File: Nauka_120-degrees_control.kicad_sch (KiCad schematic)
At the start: 0 parts

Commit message: VER1.0: накидал схему управления затворами
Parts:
- added C1, C2: 20p, Capacitor_SMD:C_0805_2012Metric_Pad1.18x1.45mm_HandSolder, symbol Device:C_Small
- added C3, C4, C5, C6, C7: 100n, Capacitor_SMD:C_0805_2012Metric_Pad1.18x1.45mm_HandSolder, symbol Device:C_Small
- added D1, D2: ~, Package_SO:SOIC-14_3.9x8.7mm_P1.27mm, symbol Logic_my:74HC32
- added R1: 10M, Resistor_SMD:R_0805_2012Metric_Pad1.20x1.40mm_HandSolder, symbol Device:R_Small
- added R2: 100k, Resistor_SMD:R_0805_2012Metric_Pad1.20x1.40mm_HandSolder, symbol Device:R_Small
- added R3, R4, R5, R6, R7, R8, R9: 0, Resistor_SMD:R_0805_2012Metric_Pad1.20x1.40mm_HandSolder, symbol Device:R_Small
- added U1: 4040, Package_SO:SO-16_3.9x9.9mm_P1.27mm, symbol 4xxx:4040
- added U2: 4017, Package_SO:SO-16_3.9x9.9mm_P1.27mm, symbol 4xxx:4017
- added U4: 74LVC2G04, symbol 74xGxx:74LVC2G04
- added Y1: 4.9152M, Crystal:Crystal_SMD_HC49-SD_HandSoldering, symbol Device:Crystal
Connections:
- new net: C1.2, R1.1, U4.1, Y1.2
- new net: R1.2, R2.1, U4.3, U4.6
- new net: C2.2, R2.2, Y1.1
- new net: R6.1, U1.14 (Q9)
- new net: R5.2, R6.2, R7.2, R8.2, U2.14 (CLK)
- new net: D1.1 (1A), D2.5 (Q10), U2.3 (Q0)
- new net: D1.10 (Q10), D2.4 (Q11), U2.1 (Q5)
- new net: D1.2 (1B), D2.10 (Q10), U2.2 (Q1)
- new net: D1.4 (Q11), D2.9 (Q11), U2.4 (Q2)
- new net: D1.5 (Q10), D2.2 (1B), U2.7 (Q3)
- new net: D1.9 (Q11), D2.1 (1A), U2.10 (Q4)
- new net: R9.1, U2.13 (CKEN)
- new net: U2.15 (Reset), U2.5 (Q6)
- new net: R8.1, U1.1 (Q11)
- new net: U1.10 (CLK), U4.4
- new net: R3.1, R4.1, U1.11 (Reset)
- new net: R5.1, U1.12 (Q8)
- new net: R7.1, U1.15 (Q10)
- new net +5V: C3.2, C4.2, C5.2, C6.2, C7.2, D1.14 (VCC), D2.14 (VCC), U1.16 (VDD), U2.16 (VDD), U4.5 (VCC)
- new net G1H: D1.3 (1Y)
- new net G1L: D2.3 (1Y)
- new net G2H: D1.6
- new net G2L: D2.6
- new net G3H: D1.8
- new net G3L: D2.8
- new net GND: C1.1, C2.1, C3.1, C4.1, C5.1, C6.1, C7.1, D1.7 (GND), D2.7 (GND), R3.2, R9.2, U1.8 (VSS), U2.8 (VSS), U4.2 (GND)
- new net Reset_4040: R4.2
- no-connect marks 0 -> 18

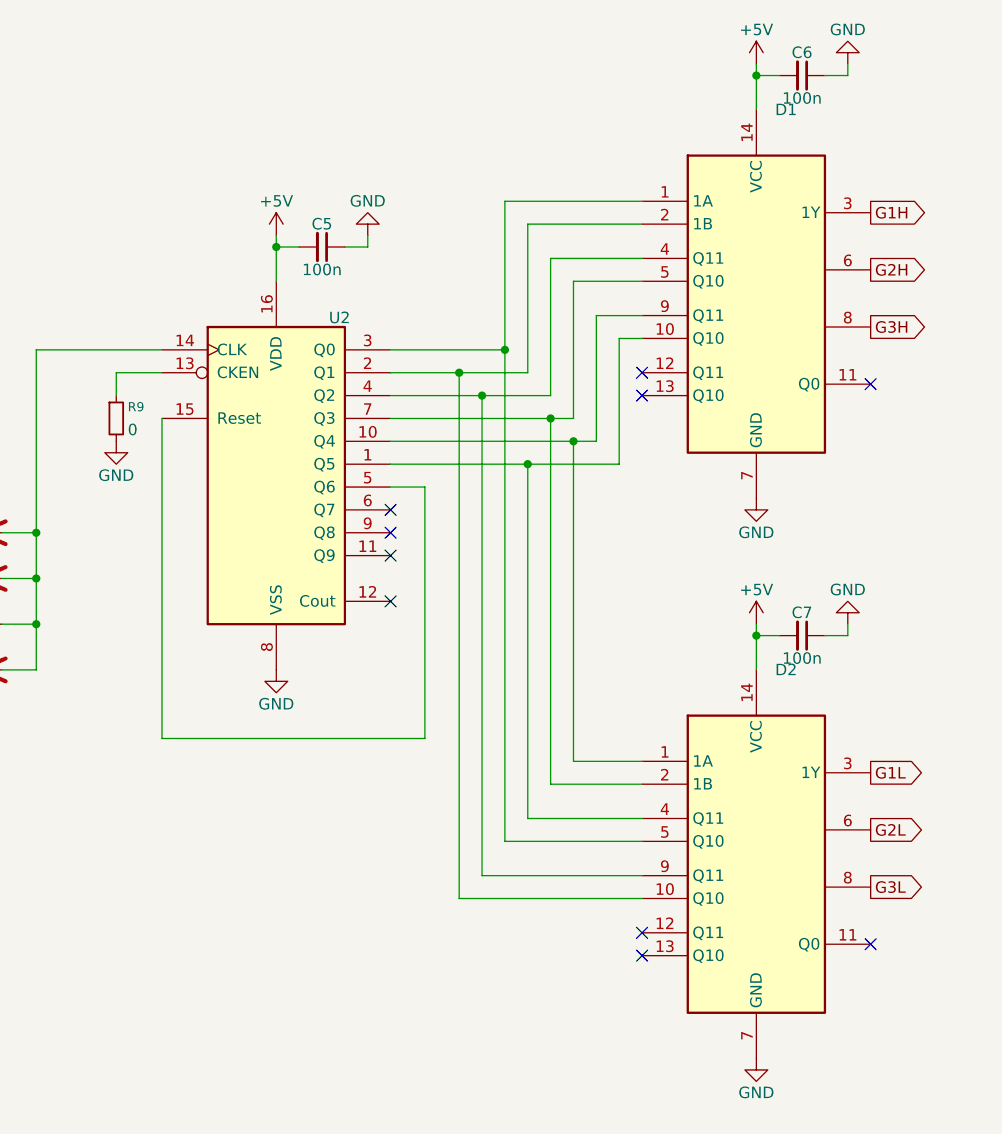
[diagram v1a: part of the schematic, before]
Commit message: VER1.0: изменил логические И на трехвходные И-НЕ
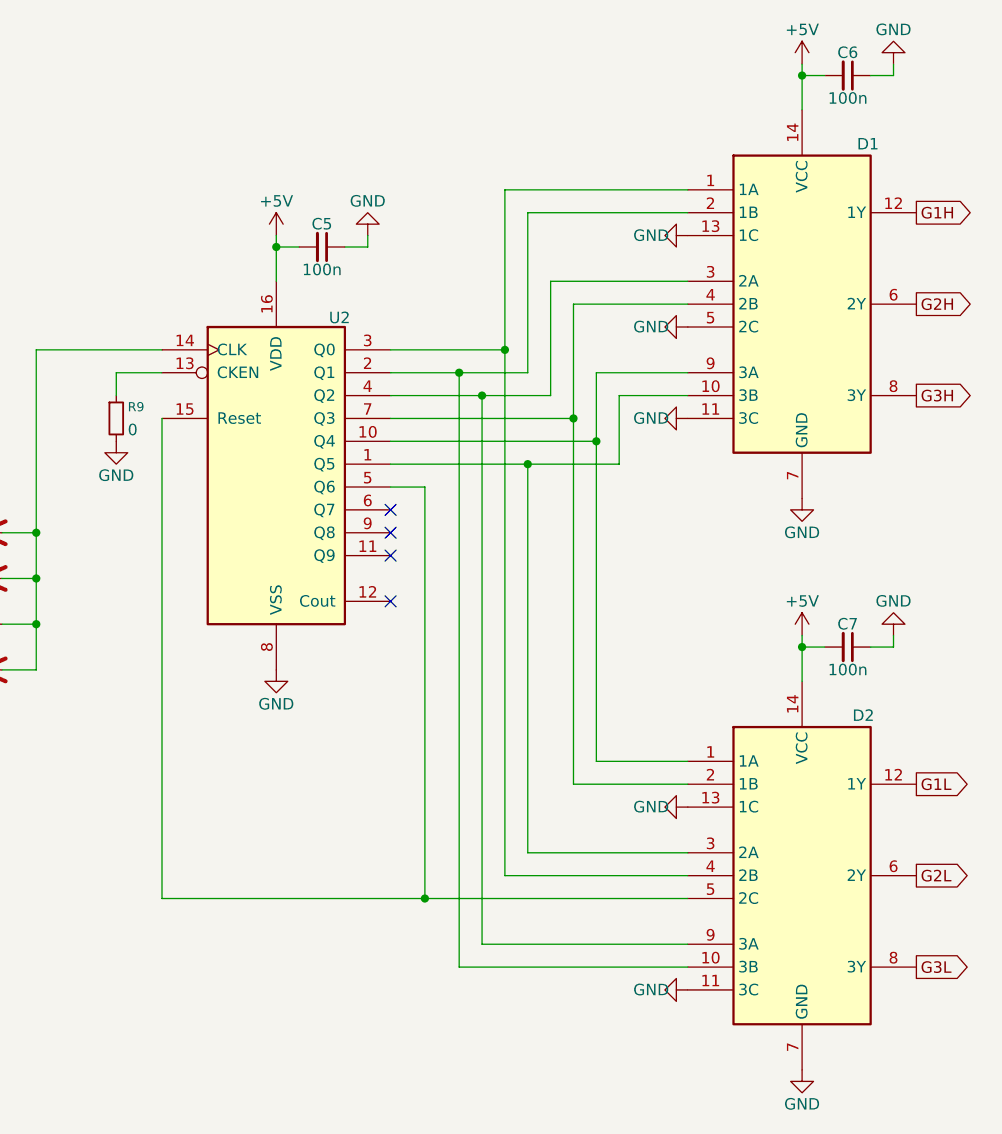
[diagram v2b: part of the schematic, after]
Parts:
- removed D1, D2: ~, Package_SO:SOIC-14_3.9x8.7mm_P1.27mm, symbol Logic_my:74HC32
- added D1, D2: ~, Package_SO:SOIC-14_3.9x8.7mm_P1.27mm, symbol Logic_my:74HC27D
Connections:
- net +5V: now also D1.14 (VCC), D2.14 (VCC)
- net G1H: now also D1.12 (1Y)
- net G1L: now also D2.12 (1Y)
- net G2H: now also D1.6 (2Y)
- net G2L: now also D2.6 (2Y)
- net G3H: now also D1.8 (3Y)
- net G3L: now also D2.8 (3Y)
- net GND: now also D1.11 (3C), D1.13 (1C), D1.5 (2C), D1.7 (GND), D2.11 (3C), D2.13 (1C), D2.7 (GND)
- net at U2.3 (Q0): now also D1.1 (1A), D2.4 (2B)
- net at U2.1 (Q5): now also D1.10 (3B), D2.3 (2A)
- net at U2.2 (Q1): now also D1.2 (1B), D2.10 (3B)
- net at U2.4 (Q2): now also D1.3 (2A), D2.9 (3A)
- net at U2.7 (Q3): now also D1.4 (2B), D2.2 (1B)
- net at U2.10 (Q4): now also D1.9 (3A), D2.1 (1A)
- net at U2.15 (Reset), U2.5 (Q6): now also D2.5 (2C)
- no-connect marks 18 -> 12
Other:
- moved on the sheet: C6, C7

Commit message: VER1.0: добавил драйвера
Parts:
- added C10, C11, C18, C19, C22, C23, C29, C30, C33, C34, C39, C40, C44, C45, C50, C51, C55, C56, C61, C62, C66, C67, C72, C73: 10u, Capacitor_SMD:C_1206_3216Metric_Pad1.33x1.80mm_HandSolder, symbol Device:C_Small
- added C13, C24, C35, C46, C57, C68: 2.2u, Capacitor_SMD:C_0805_2012Metric_Pad1.18x1.45mm_HandSolder, symbol Device:C_Small
- added C14, C25, C36, C47, C58, C69: 100p, Capacitor_SMD:C_0805_2012Metric_Pad1.18x1.45mm_HandSolder, symbol Device:C_Small
- added C15, C16, C20, C21, C42, C43, C53, C54, C6, C64, C65, C7: 4.7u, Capacitor_SMD:C_1206_3216Metric_Pad1.33x1.80mm_HandSolder, symbol Device:C_Small
- added C17, C26, C38, C48, C60, C70: 10n, Capacitor_SMD:C_0805_2012Metric_Pad1.18x1.45mm_HandSolder, symbol Device:C_Small
- added C27, C28, C31, C32, C37, C41, C49, C52, C59, C63, C71, C74: 56p, Capacitor_SMD:C_0805_2012Metric_Pad1.18x1.45mm_HandSolder, symbol Device:C_Small
- added C4: 100n, Capacitor_SMD:C_0805_2012Metric_Pad1.18x1.45mm_HandSolder, symbol Device:C_Small
- added D10, D12, D26, D33, D4, D40: NSI6651, Package_SO:SOIC-16W_7.5x10.3mm_P1.27mm, symbol Driver_My:NSI6651
- added D11, D2, D25, D32, D39, D9: ~, QAxCx, symbol Mornsun:QAxCx
- added D13, D14, D20, D21, D27, D28, D34, D35, D41, D42, D5, D6: D_Small, Diode_SMD:D_SMA_Handsoldering, symbol Device:D_Small
- added D15, D23, D30, D37, D44, D8: ~, Diode_SMD:D_SOD-123, symbol Device:D_Schottky_Small
- added D16, D17, D18, D19, D22, D24, D29, D31, D36, D38, D43, D45: ~, LED_SMD:LED_0805_2012Metric_Pad1.15x1.40mm_HandSolder, symbol Device:LED_Small
- added D3: ~, Package_SO:SO-14_3.9x8.65mm_P1.27mm, symbol Logic_my:74AHC14D
- added L1, L11, L3, L5, L7, L9: 12u, Inductor_SMD:L_1210_3225Metric_Pad1.42x2.65mm_HandSolder, symbol Device:L_Small
- added L10, L12, L2, L4, L6, L8: 47u, Inductor_SMD:L_1812_4532Metric_Pad1.30x3.40mm_HandSolder, symbol Device:L_Small
- added Q1, Q2, Q3, Q4, Q5, Q6: C2M0280120D, Package_TO_SOT_THT:TO-247-3_Horizontal_TabUp, symbol Transistor_FET:C2M0280120D
- added R10, R15, R20, R40, R50, R60: 510, Resistor_SMD:R_0805_2012Metric_Pad1.20x1.40mm_HandSolder, symbol Device:R_Small
- added R11, R16, R18, R21, R25, R27, R30, R33, R39, R41, R43, R49, R51, R53, R59, R61, R63, R69: 1k, Resistor_SMD:R_0805_2012Metric_Pad1.20x1.40mm_HandSolder, symbol Device:R_Small
- added R12, R17, R22, R42, R52, R62: Rdesat, Resistor_SMD:R_0805_2012Metric_Pad1.20x1.40mm_HandSolder, symbol Device:R_Small
- added R13, R14, R23, R24, R34, R35, R44, R45, R54, R55, R64, R65: 3, Resistor_SMD:R_0805_2012Metric_Pad1.20x1.40mm_HandSolder, symbol Device:R_Small
- added R19, R26, R29, R31, R36, R37, R46, R47, R56, R57, R66, R67: 10k, Resistor_SMD:R_0805_2012Metric_Pad1.20x1.40mm_HandSolder, symbol Device:R_Small
- added R28, R32, R38, R48, R58, R68: 560, Resistor_SMD:R_0805_2012Metric_Pad1.20x1.40mm_HandSolder, symbol Device:R_Small
- renumbered C6 to C1, C7 to C12, C4 to C2, C5 to C3, C3 to C5, C1 to C8, C2 to C9, D2 to D7, R9 to R3, R3 to R5, R5 to R6, R6 to R7, R7 to R8, R8 to R9, U4 to U1, U1 to U2, U2 to U3
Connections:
- net +5V: now also C13.2, C24.2, C35.2, C4.2, C46.2, C57.2, C68.2, D10.15 (Vcc1), D12.15 (Vcc1), D26.15 (Vcc1), D3.14 (VCC), D33.15 (Vcc1), D4.15 (Vcc1), D40.15 (Vcc1), R18.2, R25.2, R26.2, R27.2, R30.2, R31.2, R33.2, R36.2, R39.2, R43.2, R46.2, R49.2, R53.2, R56.2, R59.2, R63.2, R66.2, R69.2
- net G1H: now also D3.2 (1Y); no longer D1.12 (1Y)
- net G1L: now also D3.8 (4Y); no longer D7.12 (1Y)
- net G2H: now also D3.4 (2Y); no longer D1.6 (2Y)
- net G2L: now also D3.10 (5Y); no longer D7.6 (2Y)
- net G3H: now also D3.6 (3Y); no longer D1.8 (3Y)
- net G3L: now also D3.12 (6Y); no longer D7.8 (3Y)
- net GND: now also C13.1, C24.1, C27.2, C28.2, C31.2, C32.2, C35.1, C37.2, C4.1, C41.2, C46.1, C49.2, C52.2, C57.1, C59.2, C63.2, C68.1, C71.2, C74.2, D10.16 (TEST), D10.9 (GND1), D12.16 (TEST), D12.9 (GND1), D17.1 (K), D19.1 (K), D24.1 (K), D26.16 (TEST), D26.9 (GND1), D3.7 (GND), D31.1 (K), D33.16 (TEST), D33.9 (GND1), D38.1 (K), D4.16 (TEST), D4.9 (GND1), D40.16 (TEST), D40.9 (GND1), D45.1 (K)
- new net: D10.6 (OUTL), R35.1
- new net: D43.2 (A), R63.1
- new net: C37.1, D10.13 (~{FLT}), D22.1 (K), R36.1
- new net: D22.2 (A), R18.1
- new net: D36.2 (A), R53.1
- new net: D26.4 (OUTH), R44.1
- new net: C54.1, L10.1, L9.2
- new net: D32.1 (Vin), L10.2
- new net: C69.2, D40.2 (DESAT), D44.1 (K), R61.1
- new net: D5.1 (K), D6.2 (A)
- new net: D5.2 (A), R12.1
- new net: D17.2 (A), R28.1
- new net: C27.1, D12.12 (RDY), R25.1, R28.2
- new net: C21.1, L3.2, L4.1
- new net: D11.1 (Vin), L4.2
- new net: C36.2, D10.2 (DESAT), D23.1 (K), R16.1
- new net: D40.6 (OUTL), R65.1
- new net: C31.1, D18.1 (K), D4.13 (~{FLT}), R31.1
- new net: C52.1, D26.12 (RDY), R48.2, R49.1
- new net: C49.1, D26.13 (~{FLT}), D29.1 (K), R46.1
- new net: C47.2, D26.2 (DESAT), D30.1 (K), R41.1
- new net: D26.6 (OUTL), R45.1
- new net: D27.1 (K), D28.2 (A)
- new net: D27.2 (A), R42.1
- new net: R10.1, R11.2, R12.2
- new net: C7.1, L1.2, L2.1
- new net: D34.2 (A), R52.1
- new net: R50.1, R51.2, R52.2
- new net: C25.2, D12.2 (DESAT), D15.1 (K), R21.1
- new net: R60.1, R61.2, R62.2
- new net: C63.1, D33.12 (RDY), R58.2, R59.1
- new net: C16.1, L5.2, L6.1
- new net: D9.1 (Vin), L6.2
- new net: C65.1, L11.2, L12.1
- new net: D39.1 (Vin), L12.2
- new net: C41.1, D10.12 (RDY), R38.2, R39.1
- new net: D45.2 (A), R68.1
- new net: C43.1, L7.2, L8.1
- new net: C74.1, D40.12 (RDY), R68.2, R69.1
- new net: C71.1, D40.13 (~{FLT}), D43.1 (K), R66.1
- new net: D40.4 (OUTH), R64.1
- new net: D2.1 (Vin), L2.2
- new net: D41.2 (A), R62.1
- new net: D13.1 (K), D14.2 (A)
- new net: C14.2, D4.2 (DESAT), D8.1 (K), R11.1
- new net: C28.1, D12.13 (~{FLT}), D16.1 (K), R26.1
- new net: D12.4 (OUTH), R23.1
- new net: D12.6 (OUTL), R24.1
- new net: D18.2 (A), R30.1
- new net: C59.1, D33.13 (~{FLT}), D36.1 (K), R56.1
- new net: D19.2 (A), R32.1
- new net: C32.1, D4.12 (RDY), R32.2, R33.1
- new net: D16.2 (A), R27.1
- new net: D3.9 (4A), D7.12 (1Y)
- new net: D3.11 (5A), D7.6 (2Y)
- new net: D3.13 (6A), D7.8 (3Y)
- new net: R15.1, R16.2, R17.2
- new net: D31.2 (A), R48.1
- new net: D13.2 (A), R22.1
- new net: R40.1, R41.2, R42.2
- new net: R20.1, R21.2, R22.2
- new net: D24.2 (A), R38.1
- new net: D25.1 (Vin), L8.2
- new net: D1.12 (1Y), D3.1 (1A)
- new net: D1.6 (2Y), D3.3 (2A)
- new net: D1.8 (3Y), D3.5 (3A)
- new net: D20.2 (A), R17.1
- new net: C58.2, D33.2 (DESAT), D37.1 (K), R51.1
- new net: D41.1 (K), D42.2 (A)
- new net: D38.2 (A), R58.1
- new net: D4.4 (OUTH), R13.1
- new net: D4.6 (OUTL), R14.1
- new net: D33.4 (OUTH), R54.1
- new net: D29.2 (A), R43.1
- new net: D10.4 (OUTH), R34.1
- new net: D34.1 (K), D35.2 (A)
- new net: D20.1 (K), D21.2 (A)
- new net: D33.6 (OUTL), R55.1
- new net +15V: C15.1, C20.1, C42.1, C53.1, C6.1, C64.1, L1.1, L11.1, L3.1, L5.1, L7.1, L9.1
- new net +15VL: C22.2, C23.2, C44.2, C45.2, C66.2, C67.2, D11.7 (+Vo), D12.5 (Vcc2), D25.7 (+Vo), D26.5 (Vcc2), D39.7 (+Vo), D40.5 (Vcc2), R20.2, R40.2, R60.2
- new net +15V_H1: C10.2, C11.2, C33.2, C34.2, C55.2, C56.2, D10.5 (Vcc2), D2.7 (+Vo), D32.7 (+Vo), D33.5 (Vcc2), D4.5 (Vcc2), D9.7 (+Vo), R10.2, R15.2, R50.2
- new net -15VL: C29.1, C30.1, C50.1, C51.1, C72.1, C73.1, D11.5 (-Vo), D12.1 (Vee2), D12.8 (Vee2), D25.5 (-Vo), D26.1 (Vee2), D26.8 (Vee2), D39.5 (-Vo), D40.1 (Vee2), D40.8 (Vee2)
- new net -4V_H1: C18.1, C19.1, C39.1, C40.1, C61.1, C62.1, D10.1 (Vee2), D10.8 (Vee2), D2.5 (-Vo), D32.5 (-Vo), D33.1 (Vee2), D33.8 (Vee2), D4.1 (Vee2), D4.8 (Vee2), D9.5 (-Vo)
- new net GND1: C15.2, C16.2, C20.2, C21.2, C42.2, C43.2, C53.2, C54.2, C6.2, C64.2, C65.2, C7.2, D11.2 (GND), D2.2 (GND), D25.2 (GND), D32.2 (GND), D39.2 (GND), D9.2 (GND)
- new net GNDPWR: C22.1, C23.1, C25.1, C26.2, C29.2, C30.2, C44.1, C45.1, C47.1, C48.2, C50.2, C51.2, C66.1, C67.1, C69.1, C70.2, C72.2, C73.2, D11.6 (0V), D12.3 (GND2), D15.2 (A), D25.6 (0V), D26.3 (GND2), D30.2 (A), D39.6 (0V), D40.3 (GND2), D44.2 (A), Q2.3 (S), Q4.3 (S), Q6.3 (S), R29.1, R47.1, R67.1
- new net GND_H1: C10.1, C11.1, C14.1, C17.2, C18.2, C19.2, C33.1, C34.1, C36.1, C38.2, C39.2, C40.2, C55.1, C56.1, C58.1, C60.2, C61.2, C62.2, D10.3 (GND2), D14.1 (K), D2.6 (0V), D23.2 (A), D28.1 (K), D32.6 (0V), D33.3 (GND2), D37.2 (A), D4.3 (GND2), D42.1 (K), D8.2 (A), D9.6 (0V), Q1.3 (S), Q2.2 (D), Q3.3 (S), Q4.2 (D), Q5.3 (S), Q6.2 (D), R19.1, R37.1, R57.1
- new net GateH1: C17.1, C38.1, C60.1, D10.7 (CLAMP), D33.7 (CLAMP), D4.7 (CLAMP), Q1.1 (G), Q3.1 (G), Q5.1 (G), R13.2, R14.2, R19.2, R34.2, R35.2, R37.2, R54.2, R55.2, R57.2
- new net GateL1: C26.1, C48.1, C70.1, D12.7 (CLAMP), D26.7 (CLAMP), D40.7 (CLAMP), Q2.1 (G), Q4.1 (G), Q6.1 (G), R23.2, R24.2, R29.2, R44.2, R45.2, R47.2, R64.2, R65.2, R67.2
- new net PWM_N: D10.10 (IN+), D12.10 (IN+), D26.10 (IN+), D33.10 (IN+), D4.10 (IN+), D40.10 (IN+)
- new net PWM_P: D10.11 (IN-), D12.11 (IN-), D26.11 (IN-), D33.11 (IN-), D4.11 (IN-), D40.11 (IN-)
- new net RST: D10.14 (~{RST}), D12.14 (~{RST}), D26.14 (~{RST}), D33.14 (~{RST}), D4.14 (~{RST}), D40.14 (~{RST})
- new net VDC: D21.1 (K), D35.1 (K), D6.1 (K), Q1.2 (D), Q3.2 (D), Q5.2 (D)
